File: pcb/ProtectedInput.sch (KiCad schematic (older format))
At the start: 3 parts

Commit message: first version of the new feature set
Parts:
- C14: renamed from C17; footprint Capacitor_SMD:C_0805_2012Metric_Pad1.15x1.40mm_HandSolder -> Capacitor_SMD:C_0805_2012Metric
- R18: renamed from R13; footprint Resistor_SMD:R_0805_2012Metric_Pad1.15x1.40mm_HandSolder -> Resistor_SMD:R_0805_2012Metric
- R19: renamed from R14; footprint Resistor_SMD:R_0805_2012Metric_Pad1.15x1.40mm_HandSolder -> Resistor_SMD:R_0805_2012Metric
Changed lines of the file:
@@
 $Descr A4 11693 8268
 encoding utf-8
-Sheet 6 7
+Sheet 10 17
 Title ""
 Date ""
@@
 input
 $Comp
-L Device:R R13
+L Device:R R18
 U 1 1 5C4E78E9
 P 3200 2300
-AR Path="/5C4EB24D/5C4E78E9" Ref="R13"  Part="1"
-AR Path="/5C4EB277/5C4E78E9" Ref="R15"  Part="1"
+AR Path="/5C4EB24D/5C4E78E9" Ref="R18"  Part="1"
+AR Path="/5C4EB277/5C4E78E9" Ref="R20"  Part="1"
 AR Path="/5C4EB28C/5C4E78E9" Ref="R?"  Part="1"
-F 0 "R15" V 2993 2300 50  0000 C CNN
+AR Path="/5C9B01EE/5C4E78E9" Ref="R31"  Part="1"
+AR Path="/5C9B01F3/5C4E78E9" Ref="R?"  Part="1"
+AR Path="/5CD0B67B/5C4E78E9" Ref="R?"  Part="1"
+F 0 "R31" V 2993 2300 50  0000 C CNN
 F 1 "2.4k" V 3084 2300 50  0000 C CNN
-F 2 "Resistor_SMD:R_0805_2012Metric_Pad1.15x1.40mm_HandSolder" V 3130 2300 50  0001 C CNN
+F 2 "Resistor_SMD:R_0805_2012Metric" V 3130 2300 50  0001 C CNN
 F 3 "~" H 3200 2300 50  0001 C CNN
 	1    3200 2300
@@
 $EndComp
 $Comp
-L Device:R R14
+L Device:R R19
 U 1 1 5C4E791C
 P 4150 2450
-AR Path="/5C4EB24D/5C4E791C" Ref="R14"  Part="1"
-AR Path="/5C4EB277/5C4E791C" Ref="R16"  Part="1"
+AR Path="/5C4EB24D/5C4E791C" Ref="R19"  Part="1"
+AR Path="/5C4EB277/5C4E791C" Ref="R21"  Part="1"
 AR Path="/5C4EB28C/5C4E791C" Ref="R?"  Part="1"
-F 0 "R16" H 4220 2496 50  0000 L CNN
+AR Path="/5C9B01EE/5C4E791C" Ref="R32"  Part="1"
+AR Path="/5C9B01F3/5C4E791C" Ref="R?"  Part="1"
+AR Path="/5CD0B67B/5C4E791C" Ref="R?"  Part="1"
+F 0 "R32" H 4220 2496 50  0000 L CNN
 F 1 "620" H 4220 2405 50  0000 L CNN
-F 2 "Resistor_SMD:R_0805_2012Metric_Pad1.15x1.40mm_HandSolder" V 4080 2450 50  0001 C CNN
+F 2 "Resistor_SMD:R_0805_2012Metric" V 4080 2450 50  0001 C CNN
 F 3 "~" H 4150 2450 50  0001 C CNN
 	1    4150 2450
@@
 $EndComp
 $Comp
-L Device:C C17
+L Device:C C14
 U 1 1 5C4E7961
 P 4700 2450
-AR Path="/5C4EB24D/5C4E7961" Ref="C17"  Part="1"
-AR Path="/5C4EB277/5C4E7961" Ref="C18"  Part="1"
+AR Path="/5C4EB24D/5C4E7961" Ref="C14"  Part="1"
+AR Path="/5C4EB277/5C4E7961" Ref="C15"  Part="1"
 AR Path="/5C4EB28C/5C4E7961" Ref="C?"  Part="1"
-F 0 "C18" H 4815 2496 50  0000 L CNN
+AR Path="/5C9B01EE/5C4E7961" Ref="C24"  Part="1"
+AR Path="/5C9B01F3/5C4E7961" Ref="C?"  Part="1"
+AR Path="/5CD0B67B/5C4E7961" Ref="C?"  Part="1"
+F 0 "C24" H 4815 2496 50  0000 L CNN
 F 1 "1n" H 4815 2405 50  0000 L CNN
-F 2 "Capacitor_SMD:C_0805_2012Metric_Pad1.15x1.40mm_HandSolder" H 4738 2300 50  0001 C CNN
+F 2 "Capacitor_SMD:C_0805_2012Metric" H 4738 2300 50  0001 C CNN
 F 3 "~" H 4700 2450 50  0001 C CNN
 	1    4700 2450

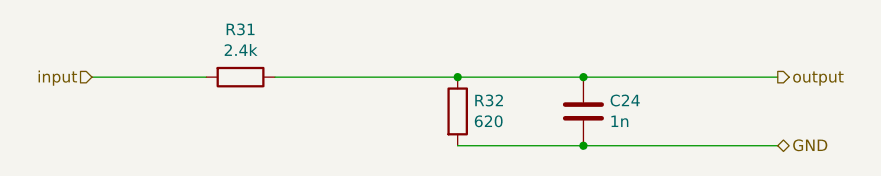
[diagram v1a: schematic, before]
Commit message: Changed some values - RC for the inputs to lower frequencys, reduced lines on the BOM by some minor value changes
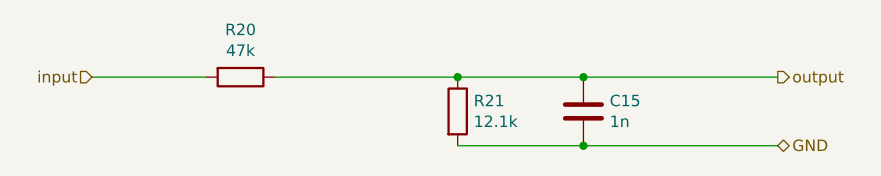
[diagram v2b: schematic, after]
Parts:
- R18: value 2.4k -> 47k
- R19: value 620 -> 12.1k
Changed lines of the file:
@@
 $Descr A4 11693 8268
 encoding utf-8
-Sheet 10 17
+Sheet 5 17
 Title ""
 Date ""
@@
 AR Path="/5C9B01F3/5C4E78E9" Ref="R?"  Part="1"
 AR Path="/5CD0B67B/5C4E78E9" Ref="R?"  Part="1"
-F 0 "R31" V 2993 2300 50  0000 C CNN
-F 1 "2.4k" V 3084 2300 50  0000 C CNN
+F 0 "R20" V 2993 2300 50  0000 C CNN
+F 1 "47k" V 3084 2300 50  0000 C CNN
 F 2 "Resistor_SMD:R_0805_2012Metric" V 3130 2300 50  0001 C CNN
 F 3 "~" H 3200 2300 50  0001 C CNN
@@
 AR Path="/5C9B01F3/5C4E791C" Ref="R?"  Part="1"
 AR Path="/5CD0B67B/5C4E791C" Ref="R?"  Part="1"
-F 0 "R32" H 4220 2496 50  0000 L CNN
-F 1 "620" H 4220 2405 50  0000 L CNN
+F 0 "R21" H 4220 2496 50  0000 L CNN
+F 1 "12.1k" H 4220 2405 50  0000 L CNN
 F 2 "Resistor_SMD:R_0805_2012Metric" V 4080 2450 50  0001 C CNN
 F 3 "~" H 4150 2450 50  0001 C CNN
@@
 AR Path="/5C9B01F3/5C4E7961" Ref="C?"  Part="1"
 AR Path="/5CD0B67B/5C4E7961" Ref="C?"  Part="1"
-F 0 "C24" H 4815 2496 50  0000 L CNN
+F 0 "C15" H 4815 2496 50  0000 L CNN
 F 1 "1n" H 4815 2405 50  0000 L CNN
 F 2 "Capacitor_SMD:C_0805_2012Metric" H 4738 2300 50  0001 C CNN

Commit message: Added an other uart for ardusimple RTK2Bligh daughterboard on top of the normal RTK2B. Removed two LEDs to free up PINs
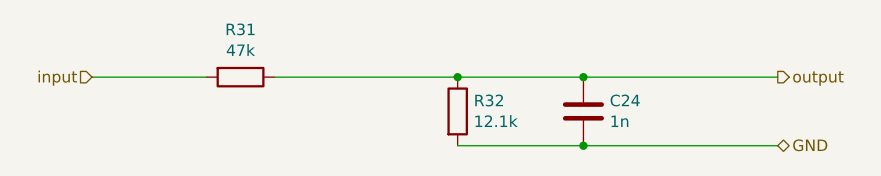
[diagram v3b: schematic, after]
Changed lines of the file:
@@
 AR Path="/5C9B01F3/5C4E78E9" Ref="R?"  Part="1"
 AR Path="/5CD0B67B/5C4E78E9" Ref="R?"  Part="1"
-F 0 "R20" V 2993 2300 50  0000 C CNN
+F 0 "R31" V 2993 2300 50  0000 C CNN
 F 1 "47k" V 3084 2300 50  0000 C CNN
 F 2 "Resistor_SMD:R_0805_2012Metric" V 3130 2300 50  0001 C CNN
@@
 AR Path="/5C9B01F3/5C4E791C" Ref="R?"  Part="1"
 AR Path="/5CD0B67B/5C4E791C" Ref="R?"  Part="1"
-F 0 "R21" H 4220 2496 50  0000 L CNN
+F 0 "R32" H 4220 2496 50  0000 L CNN
 F 1 "12.1k" H 4220 2405 50  0000 L CNN
 F 2 "Resistor_SMD:R_0805_2012Metric" V 4080 2450 50  0001 C CNN
@@
 AR Path="/5C9B01F3/5C4E7961" Ref="C?"  Part="1"
 AR Path="/5CD0B67B/5C4E7961" Ref="C?"  Part="1"
-F 0 "C15" H 4815 2496 50  0000 L CNN
+F 0 "C24" H 4815 2496 50  0000 L CNN
 F 1 "1n" H 4815 2405 50  0000 L CNN
 F 2 "Capacitor_SMD:C_0805_2012Metric" H 4738 2300 50  0001 C CNN
